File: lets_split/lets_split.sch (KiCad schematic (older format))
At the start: 62 parts, among them J1 3PIN, J2 6PIN, J3 3PIN, J4 CON1, SW1 SW_PUSH, SW10 SW_PUSH, SW11 SW_PUSH, SW12 SW_PUSH, SW13 SW_PUSH, SW14 SW_PUSH, SW15 SW_PUSH, SW16 SW_PUSH, SW17 SW_PUSH, SW18 SW_PUSH, SW19 SW_PUSH, SW2 SW_PUSH, SW20 SW_PUSH, SW21 SW_PUSH, SW22 SW_PUSH, SW23 SW_PUSH, SW24 SW_PUSH, SW3 SW_PUSH, SW4 SW_PUSH, SW5 SW_PUSH, SW6 SW_PUSH, SW7 SW_PUSH, SW8 SW_PUSH, SW9 SW_PUSH, U1 ProMicro, U2 HOLE, U3 HOLE, U4 HOLE, U5 HOLE

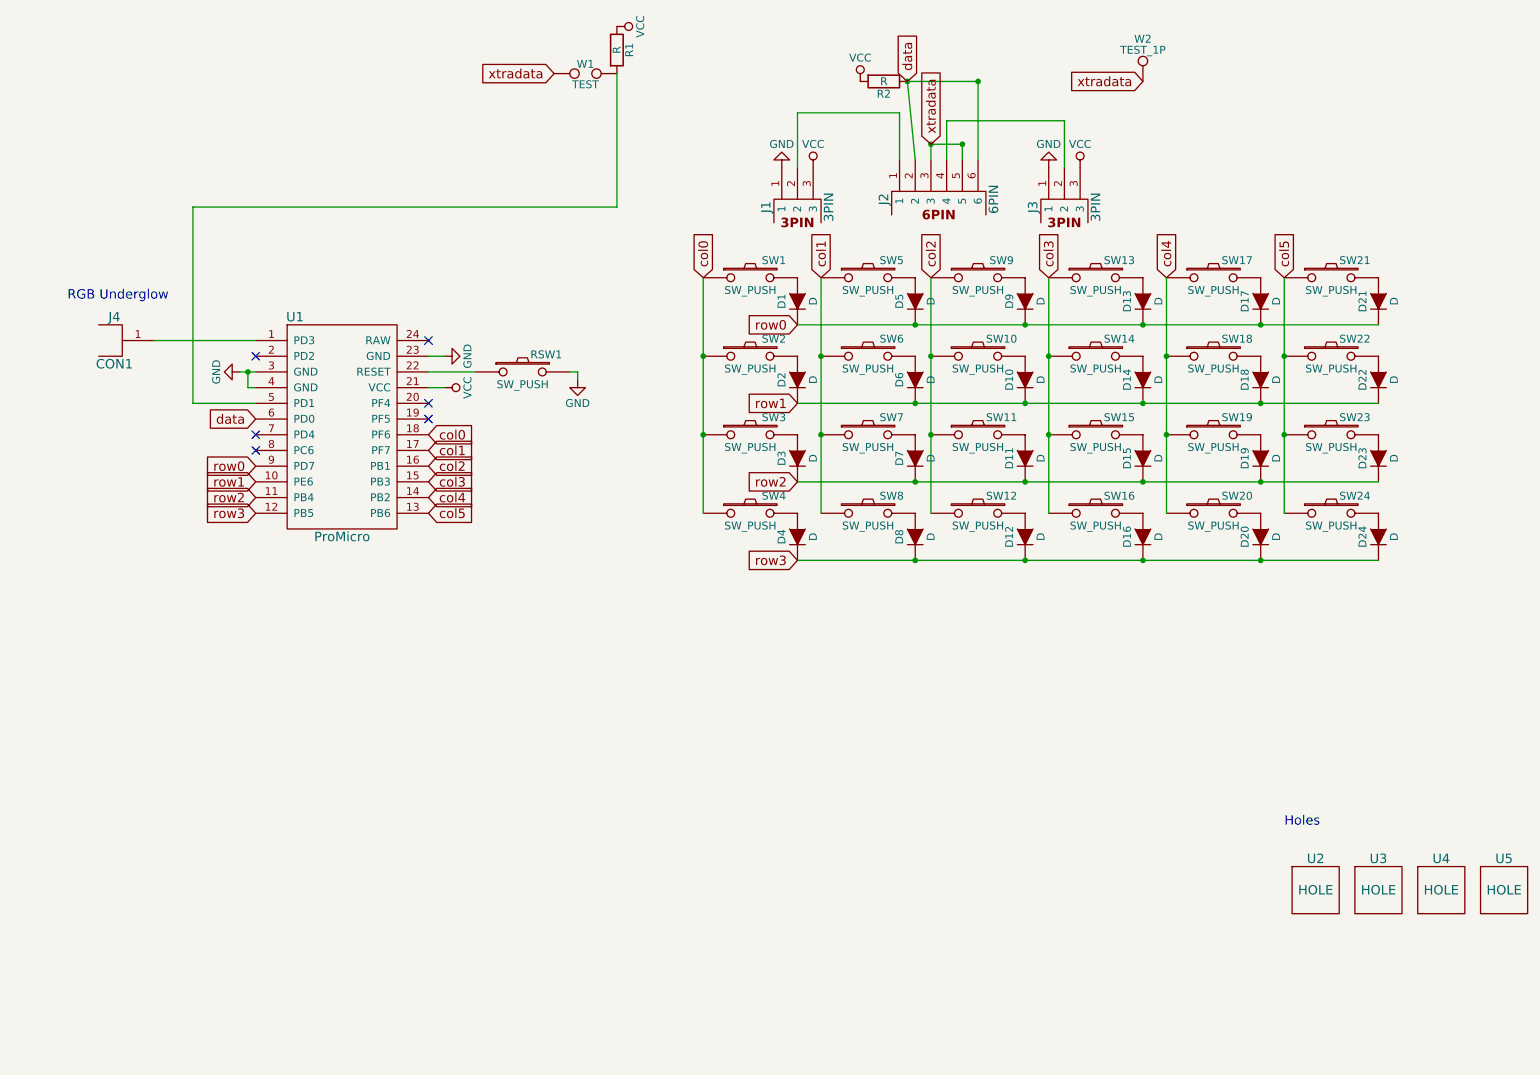
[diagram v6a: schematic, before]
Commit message: Rearrange schematic
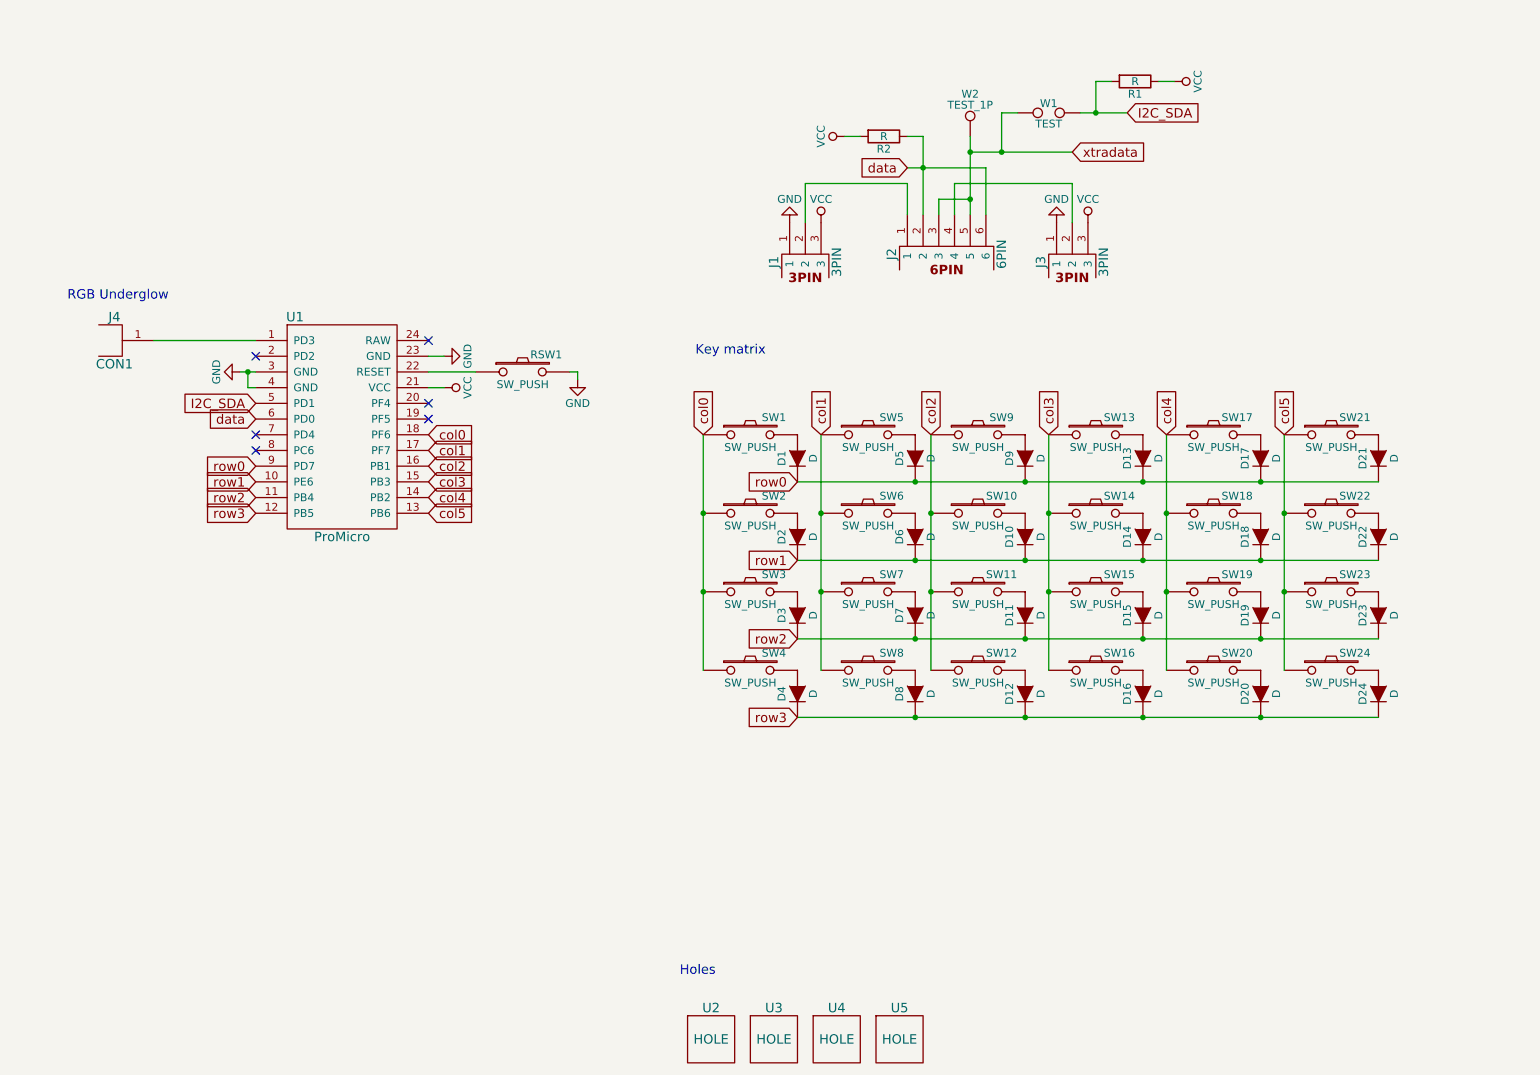
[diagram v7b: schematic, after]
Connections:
- net I2C_SDA: now reaches R1.2, U1.5 (PD1), W1.2
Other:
- note added: "Key matrix"
- moved on the sheet: D1, D10, D11, D12, D13, D14, D15, D16, D17, D18, D19, D2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

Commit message: Add pads for RGB LED strip which uses WS2812B for underglow
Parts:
- added J4, J6, J7, J8, J9: CON1, local:CON1_SMD_BOTH, symbol 1PIN
- J5: renamed from J4; footprint local:CON1 -> local:CON1_SMD_BOTH; symbol CON1 -> 1PIN
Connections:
- net GND: now also J6.1, J9.1
- net VCC: now also J4.1, J7.1
- net xtradata: now also J8.1
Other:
- moved on the sheet: J5
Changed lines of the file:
@@
 NoConn ~ 3400 3100
 $Comp
-L CON1 J4
+L 1PIN J5
 U 1 1 59A446B6
-P 1400 2600
-F 0 "J4" H 1400 2750 60  0000 C CNN
-F 1 "CON1" H 1400 2450 60  0000 C CNN
-F 2 "local:CON1" H 1350 2600 60  0001 C CNN
-F 3 "" H 1350 2600 60  0001 C CNN
-	1    1400 2600
-	1    0    0    -1
-$EndComp
-Wire Wire Line
-	2300 2600 1650 2600
-Text Notes 1100 2350 0    60   ~ 0
+P 900 2600
+F 0 "J5" H 900 2750 60  0000 C CNN
+F 1 "CON1" H 900 2450 60  0000 C CNN
+F 2 "local:CON1_SMD_BOTH" H 850 2600 60  0001 C CNN
+F 3 "" H 850 2600 60  0001 C CNN
+	1    900  2600
+	1    0    0    -1
+$EndComp
+Wire Wire Line
+	1150 2600 2300 2600
+Text Notes 750  1950 0    60   ~ 0
 RGB Underglow
 $Comp
@@
 Wire Wire Line
 	6050 1300 6150 1300
+$Comp
+L VCC #PWR011
+U 1 1 59A522C2
+P 1250 2200
+F 0 "#PWR011" H 1250 2050 50  0001 C CNN
+F 1 "VCC" H 1250 2350 50  0000 C CNN
+F 2 "" H 1250 2200 50  0000 C CNN
+F 3 "" H 1250 2200 50  0000 C CNN
+	1    1250 2200
+	0    1    1    0
+$EndComp
+$Comp
+L GND #PWR012
+U 1 1 59A523C9
+P 1250 3000
+F 0 "#PWR012" H 1250 2750 50  0001 C CNN
+F 1 "GND" H 1250 2850 50  0000 C CNN
+F 2 "" H 1250 3000 50  0000 C CNN
+F 3 "" H 1250 3000 50  0000 C CNN
+	1    1250 3000
+	0    -1   -1   0
+$EndComp
+Wire Wire Line
+	1250 3000 1150 3000
+$Comp
+L 1PIN J4
+U 1 1 59A54755
+P 900 2200
+F 0 "J4" H 900 2350 60  0000 C CNN
+F 1 "CON1" H 900 2050 60  0000 C CNN
+F 2 "local:CON1_SMD_BOTH" H 850 2200 60  0001 C CNN
+F 3 "" H 850 2200 60  0001 C CNN
+	1    900  2200
+	1    0    0    -1
+$EndComp
+$Comp
+L 1PIN J6
+U 1 1 59A547F9
+P 900 3000
+F 0 "J6" H 900 3150 60  0000 C CNN
+F 1 "CON1" H 900 2850 60  0000 C CNN
+F 2 "local:CON1_SMD_BOTH" H 850 3000 60  0001 C CNN
+F 3 "" H 850 3000 60  0001 C CNN
+	1    900  3000
+	1    0    0    -1
+$EndComp
+Wire Wire Line
+	1250 2200 1150 2200
+$Comp
+L VCC #PWR013
+U 1 1 59A52B8D
+P 1250 3600
+F 0 "#PWR013" H 1250 3450 50  0001 C CNN
+F 1 "VCC" H 1250 3750 50  0000 C CNN
+F 2 "" H 1250 3600 50  0000 C CNN
+F 3 "" H 1250 3600 50  0000 C CNN
+	1    1250 3600
+	0    1    1    0
+$EndComp
+$Comp
+L GND #PWR014
+U 1 1 59A52B93
+P 1250 4400
+F 0 "#PWR014" H 1250 4150 50  0001 C CNN
+F 1 "GND" H 1250 4250 50  0000 C CNN
+F 2 "" H 1250 4400 50  0000 C CNN
+F 3 "" H 1250 4400 50  0000 C CNN
+	1    1250 4400
+	0    -1   -1   0
+$EndComp
+Wire Wire Line
+	1250 4400 1150 4400
+$Comp
+L 1PIN J8
+U 1 1 59A52B9A
+P 900 4000
+F 0 "J8" H 900 4150 60  0000 C CNN
+F 1 "CON1" H 900 3850 60  0000 C CNN
+F 2 "local:CON1_SMD_BOTH" H 850 4000 60  0001 C CNN
+F 3 "" H 850 4000 60  0001 C CNN
+	1    900  4000
+	1    0    0    -1
+$EndComp
+$Comp
+L 1PIN J9
+U 1 1 59A52BA0
+P 900 4400
+F 0 "J9" H 900 4550 60  0000 C CNN
+F 1 "CON1" H 900 4250 60  0000 C CNN
+F 2 "local:CON1_SMD_BOTH" H 850 4400 60  0001 C CNN
+F 3 "" H 850 4400 60  0001 C CNN
+	1    900  4400
+	1    0    0    -1
+$EndComp
+Wire Wire Line
+	1250 3600 1150 3600
+$Comp
+L 1PIN J7
+U 1 1 59A52C6D
+P 900 3600
+F 0 "J7" H 900 3750 60  0000 C CNN
+F 1 "CON1" H 900 3450 60  0000 C CNN
+F 2 "local:CON1_SMD_BOTH" H 850 3600 60  0001 C CNN
+F 3 "" H 850 3600 60  0001 C CNN
+	1    900  3600
+	1    0    0    -1
+$EndComp
+Wire Wire Line
+	1150 4000 1250 4000
+Text GLabel 1250 4000 2    60   Input ~ 0
+xtradata
 $EndSCHEMATC
